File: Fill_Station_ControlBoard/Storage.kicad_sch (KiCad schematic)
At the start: 6 parts, among them J5 Micro_SD_Card_Det1

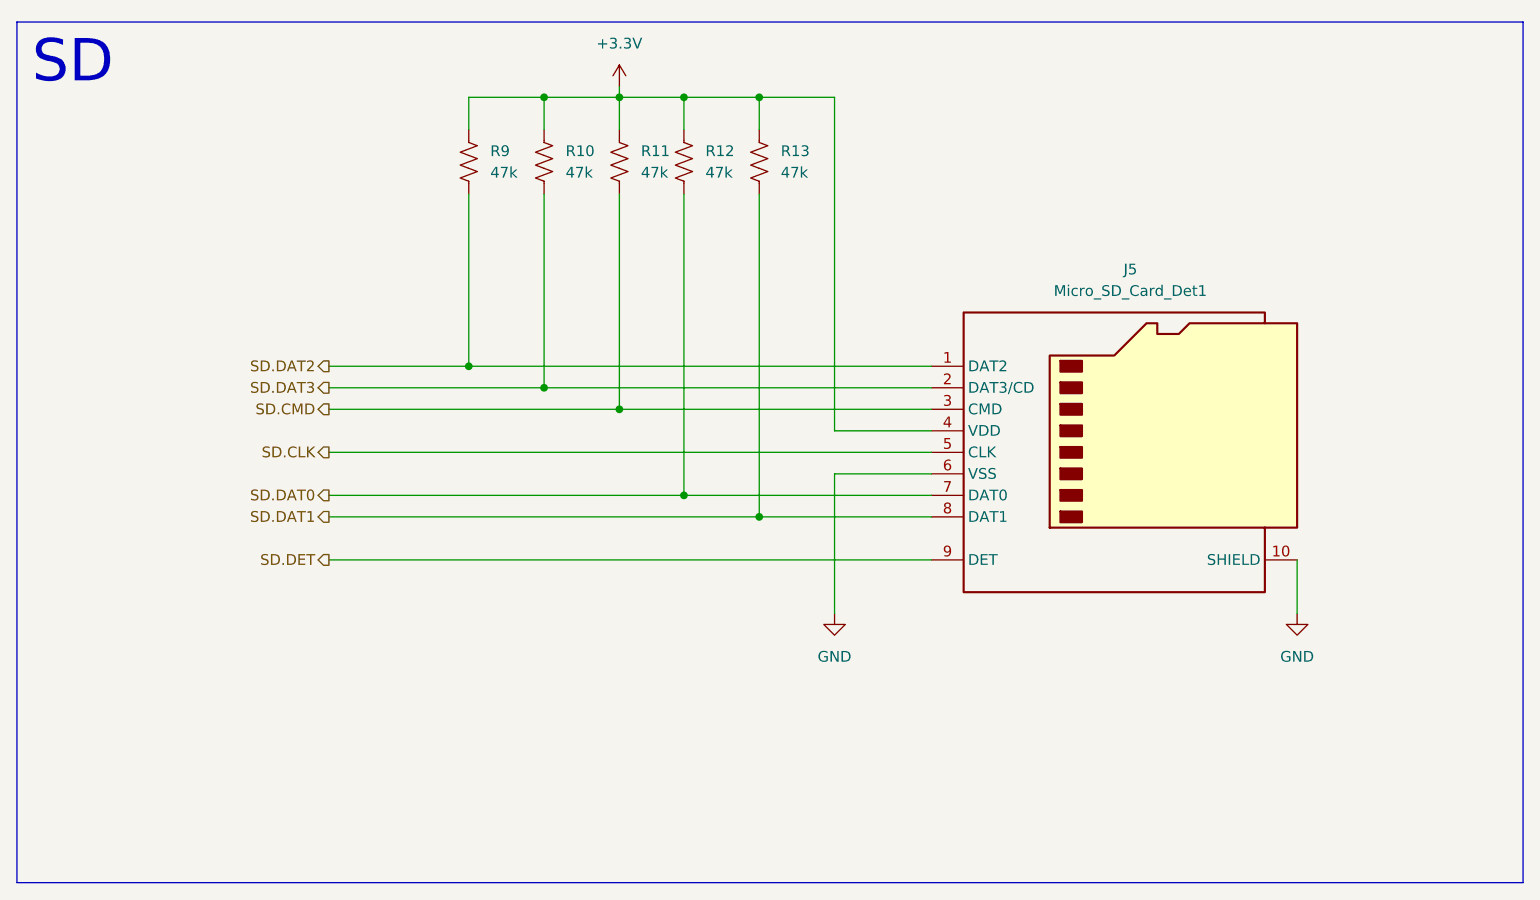
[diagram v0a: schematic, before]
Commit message: petites modifs pour ethernet + usb
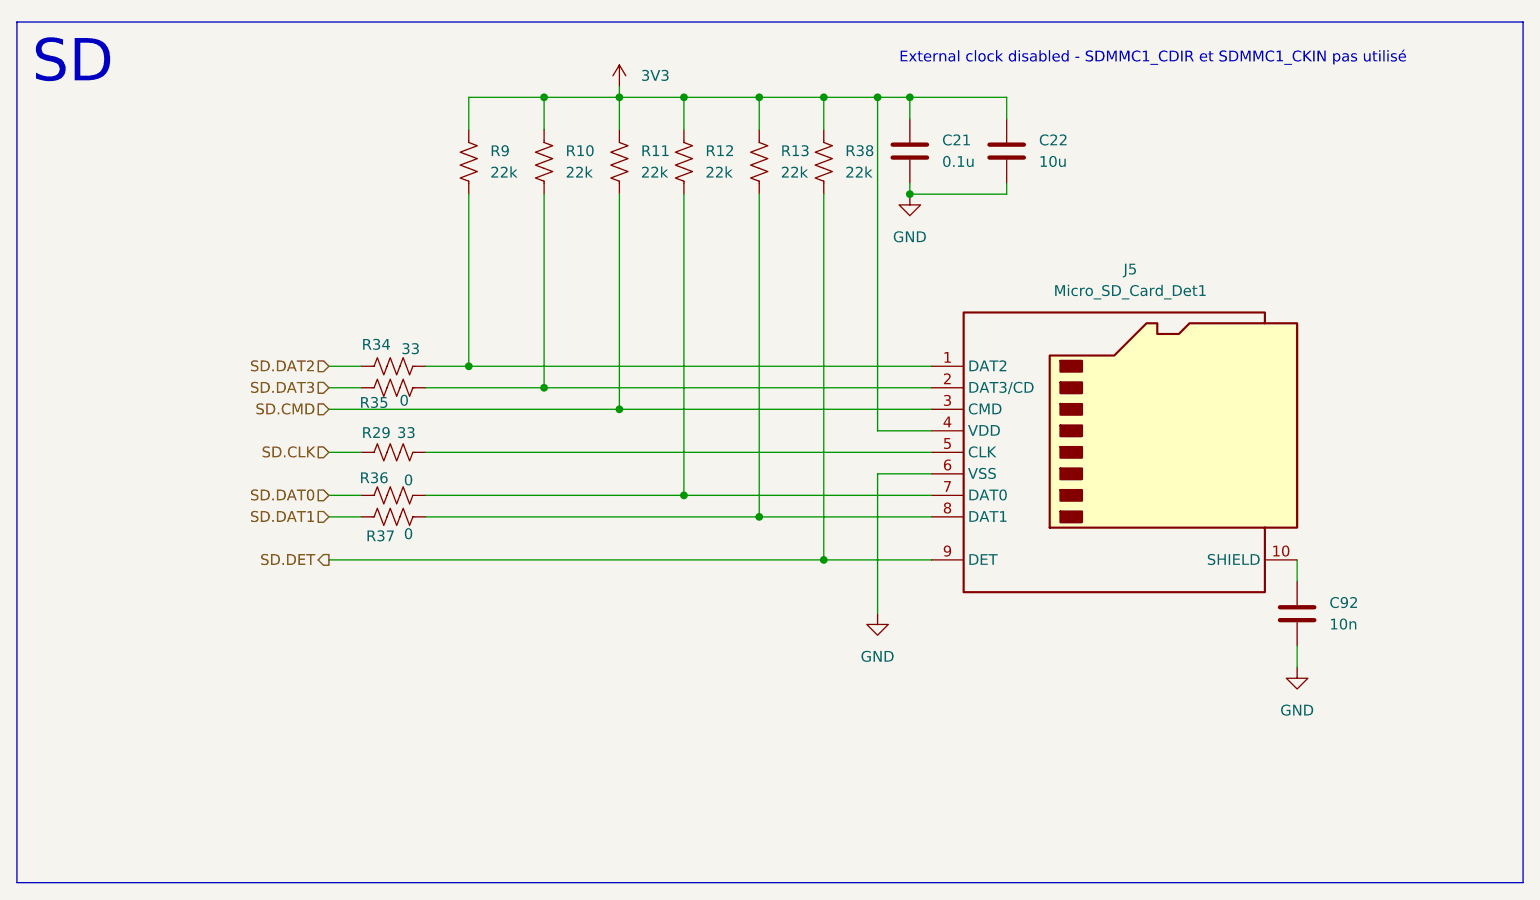
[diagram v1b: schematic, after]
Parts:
- added C21: 0.1u, symbol Device:C
- added C22: 10u, symbol Device:C
- added C92: 10n, symbol Device:C
- added R29, R34: 33, symbol Device:R_US
- added R35, R36, R37: 0, symbol Device:R_US
- added R38: 22k, symbol Device:R_US
- R10, R11, R12, R13, R9: value 47k -> 22k
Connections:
- net GND: now also C21.2, C22.2, C92.2; no longer J5.10 (SHIELD)
- net SD.CLK: now also R29.1; no longer J5.5 (CLK)
- net SD.DAT0: now also R36.1; no longer J5.7 (DAT0), R12.2
- net SD.DAT1: now also R37.1; no longer J5.8 (DAT1), R13.2
- net SD.DAT2: now also R34.1; no longer J5.1 (DAT2), R9.2
- net SD.DAT3: now also R35.1; no longer J5.2 (DAT3/CD), R10.2
- net SD.DET: now also R38.2
- net +3.3V renamed 3V3
- net 3V3: now also C21.1, C22.1, R38.1
- new net: J5.8 (DAT1), R13.2, R37.2
- new net: J5.5 (CLK), R29.2
- new net: J5.2 (DAT3/CD), R10.2, R35.2
- new net: J5.1 (DAT2), R34.2, R9.2
- new net: J5.7 (DAT0), R12.2, R36.2
- new net: C92.1, J5.10 (SHIELD)
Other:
- note added: "External clock disabled - SDMMC1_CDIR et SDMMC1_CKIN pas utilisé"

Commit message: Changement de CAN et quelques trucs
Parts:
- R10, R11, R12, R13, R29, R34, R35, R36, R37, R38, R9: footprint (none) -> Resistor_SMD:R_0603_1608Metric_Pad0.98x0.95mm_HandSolder
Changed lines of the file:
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@@
 			)
 		)
-		(property "Footprint" ""
+		(property "Footprint" "Resistor_SMD:R_0603_1608Metric_Pad0.98x0.95mm_HandSolder"
 			(at 144.526 56.134 90)
 			(effects
@@
 			)
 		)
-		(property "Footprint" ""
+		(property "Footprint" "Resistor_SMD:R_0603_1608Metric_Pad0.98x0.95mm_HandSolder"
 			(at 92.964 96.774 90)
 			(effects
@@
 			)
 		)
-		(property "Footprint" ""
+		(property "Footprint" "Resistor_SMD:R_0603_1608Metric_Pad0.98x0.95mm_HandSolder"
 			(at 92.964 89.154 90)
 			(effects
@@
 			)
 		)
-		(property "Footprint" ""
+		(property "Footprint" "Resistor_SMD:R_0603_1608Metric_Pad0.98x0.95mm_HandSolder"
 			(at 92.964 81.534 90)
 			(effects
@@
 			)
 		)
-		(property "Footprint" ""
+		(property "Footprint" "Resistor_SMD:R_0603_1608Metric_Pad0.98x0.95mm_HandSolder"
 			(at 120.396 56.134 90)
 			(effects
@@
 			)
 		)
-		(property "Footprint" ""
+		(property "Footprint" "Resistor_SMD:R_0603_1608Metric_Pad0.98x0.95mm_HandSolder"
 			(at 136.906 56.134 90)
 			(effects
@@
 			)
 		)
-		(property "Footprint" ""
+		(property "Footprint" "Resistor_SMD:R_0603_1608Metric_Pad0.98x0.95mm_HandSolder"
 			(at 92.964 78.994 90)
 			(effects
@@
 			)
 		)
-		(property "Footprint" ""
+		(property "Footprint" "Resistor_SMD:R_0603_1608Metric_Pad0.98x0.95mm_HandSolder"
 			(at 102.616 56.134 90)
 			(effects
@@
 			)
 		)
-		(property "Footprint" ""
+		(property "Footprint" "Resistor_SMD:R_0603_1608Metric_Pad0.98x0.95mm_HandSolder"
 			(at 128.016 56.134 90)
 			(effects
@@
 			)
 		)
-		(property "Footprint" ""
+		(property "Footprint" "Resistor_SMD:R_0603_1608Metric_Pad0.98x0.95mm_HandSolder"
 			(at 111.506 56.134 90)
 			(effects
@@
 			)
 		)
-		(property "Footprint" ""
+		(property "Footprint" "Resistor_SMD:R_0603_1608Metric_Pad0.98x0.95mm_HandSolder"
 			(at 92.964 94.234 90)
 			(effects

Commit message: Assignation footprint pis valeurs resistances del
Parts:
- C21, C22, C92: footprint (none) -> Capacitor_SMD:C_0603_1608Metric
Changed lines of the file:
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@@
 			)
 		)
-		(property "Footprint" ""
+		(property "Footprint" "Capacitor_SMD:C_0603_1608Metric"
 			(at 166.0652 58.42 0)
 			(effects
@@
 			)
 		)
-		(property "Footprint" ""
+		(property "Footprint" "Capacitor_SMD:C_0603_1608Metric"
 			(at 154.6352 58.42 0)
 			(effects
@@
 			)
 		)
-		(property "Footprint" ""
+		(property "Footprint" "Capacitor_SMD:C_0603_1608Metric"
 			(at 200.3552 113.03 0)
 			(effects

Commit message: Fait des trucs (commencer arrangement de pièces sur PCB
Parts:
- J5: footprint (none) -> Connector_Card:microSD_HC_Hirose_DM3AT-SF-PEJM5
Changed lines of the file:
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@@
 			)
 		)
-		(property "Footprint" ""
+		(property "Footprint" "Connector_Card:microSD_HC_Hirose_DM3AT-SF-PEJM5"
 			(at 231.14 72.39 0)
 			(effects

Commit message: arthur
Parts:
- removed C21: 0.1u, Capacitor_SMD:C_0603_1608Metric, symbol Device:C
- removed C22: 10u, Capacitor_SMD:C_0603_1608Metric, symbol Device:C
- removed C92: 10n, Capacitor_SMD:C_0603_1608Metric, symbol Device:C
- removed J5: Micro_SD_Card_Det1, Connector_Card:microSD_HC_Hirose_DM3AT-SF-PEJM5, symbol Connector:Micro_SD_Card_Det1
- removed R10, R11, R12, R13, R38, R9: 22k, Resistor_SMD:R_0603_1608Metric_Pad0.98x0.95mm_HandSolder, symbol Device:R_US
- removed R29, R34: 33, Resistor_SMD:R_0603_1608Metric_Pad0.98x0.95mm_HandSolder, symbol Device:R_US
- removed R35, R36, R37: 0, Resistor_SMD:R_0603_1608Metric_Pad0.98x0.95mm_HandSolder, symbol Device:R_US
- added C45: 0.1u, symbol Device:C
- added C46: 10u, symbol Device:C
- added C47: 10n, symbol Device:C
- added J2: Micro_SD_Card_Det1, symbol Connector:Micro_SD_Card_Det1
- added R56, R57, R58, R59, R60: 22, symbol Device:R_US
- added R61, R62, R63, R64, R65, R66: 22k, symbol Device:R_US
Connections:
- net 3V3: now also C45.1, C46.1, J2.4 (VDD), R61.1, R62.1, R63.1, R64.1, R65.1, R66.1
- net GND: now also C45.2, C46.2, C47.2, J2.6 (VSS)
- net SD.CLK: now also R58.1
- net SD.CMD: now also J2.3 (CMD), R63.2
- net SD.DAT0: now also R59.1
- net SD.DAT1: now also R60.1
- net SD.DAT2: now also R56.1
- net SD.DAT3: now also R57.1
- net SD.DET: now also J2.9 (DET), R66.2
- new net: J2.5 (CLK), R58.2
- new net: C47.1, J2.10 (SHIELD)
- new net: J2.7 (DAT0), R59.2, R64.2
- new net: J2.8 (DAT1), R60.2, R65.2
- new net: J2.2 (DAT3/CD), R57.2, R62.2
- new net: J2.1 (DAT2), R56.2, R61.2

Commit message: Modifs de l'organisation des pages
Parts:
- C45, C46: footprint (none) -> Capacitor_SMD:C_0603_1608Metric
- C47: value 10n -> 100n
- R61, R62, R63, R64, R65, R66: value 22k -> 10k
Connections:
- net 3V3: no longer C45.1, C46.1, J2.4 (VDD)
- new net: C45.1, C46.1, J2.4 (VDD)
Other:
- moved on the sheet: C45, C46, R56, R57, R58, R59, R60

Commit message: Ajout power
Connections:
- net 3V3: now also C45.1, C46.1, J2.4 (VDD)
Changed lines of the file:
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@@
+	)
+	(junction
+		(at 158.75 60.96)
+		(diameter 0)
+		(color 0 0 0 0)
 	)
 	(junction
@@
 		(pts
 			(xy 140.97 60.96) (xy 148.59 60.96)
+		)
+		(stroke
+			(width 0)
+			(type default)
+		)
+	)
+	(wire
+		(pts
+			(xy 158.75 59.69) (xy 158.75 60.96)
 		)
 		(stroke
@@
 		(on_board yes)
 		(dnp no)
-		(fields_autoplaced yes)
 		(property "Reference" "#PWR052"
 			(at 124.46 63.5 0)
@@
 		)
 		(property "Value" "3V3"
-			(at 127 58.4199 0)
+			(at 122.682 56.134 0)
 			(effects
 				(font
@@
 					(unit 1)
 				)
+			)
+		)
+	)
+	(symbol
+		(lib_id "power:+3.3V")
+		(at 158.75 59.69 0)
+		(unit 1)
+		(exclude_from_sim no)
+		(in_bom yes)
+		(on_board yes)
+		(dnp no)
+		(property "Reference" "#PWR063"
+			(at 158.75 63.5 0)
+			(effects
+				(font
+					(size 1.27 1.27)
+				)
+				(hide yes)
+			)
+		)
+		(property "Value" "3V3"
+			(at 156.972 56.134 0)
+			(effects
+				(font
+					(size 1.27 1.27)
+				)
+				(justify left)
+			)
+		)
+		(property "Footprint" ""
+			(at 158.75 59.69 0)
+			(effects
+				(font
+					(size 1.27 1.27)
+				)
+				(hide yes)
+			)
+		)
+		(property "Datasheet" ""
+			(at 158.75 59.69 0)
+			(effects
+				(font
+					(size 1.27 1.27)
+				)
+				(hide yes)
+			)
+		)
+		(property "Description" "Power symbol creates a global label with name \"+3.3V\""
+			(at 158.75 59.69 0)
+			(effects
+				(font
+					(size 1.27 1.27)
+				)
+				(hide yes)
+			)
+		)
+		(pin "1"
+		)
+		(instances
+			(project "Fill_Station_ControlBoard"
+				(path "/eaacffe0-ee57-428e-a37e-5655e0922ccc/86dfffbf-ac08-41cb-ab8f-382cca5b005c"
+					(reference "#PWR063")
+					(unit 1)
+				)
